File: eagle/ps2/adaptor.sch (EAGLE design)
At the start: 9 parts, among them T1 BSS138, T3 BSS138

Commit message: updated
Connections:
- net CLK_3V3: now also JP1.2; no longer JP1.1
- net DATA_3V3: now also JP1.1; no longer JP1.2
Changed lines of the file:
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@@
 </segment>
 <segment>
-<pinref part="JP1" gate="A" pin="1"/>
-<wire x1="73.66" y1="78.74" x2="73.66" y2="88.9" width="0.1524" layer="91"/>
-<label x="73.152" y="89.154" size="1.778" layer="95" rot="R90"/>
+<pinref part="JP1" gate="A" pin="2"/>
+<wire x1="81.28" y1="78.74" x2="81.28" y2="88.9" width="0.1524" layer="91"/>
+<label x="81.026" y="88.9" size="1.778" layer="95" rot="R90"/>
 </segment>
 </net>
@@
 </segment>
 <segment>
-<pinref part="JP1" gate="A" pin="2"/>
-<wire x1="81.28" y1="78.74" x2="81.28" y2="88.9" width="0.1524" layer="91"/>
-<label x="81.026" y="88.9" size="1.778" layer="95" rot="R90"/>
+<pinref part="JP1" gate="A" pin="1"/>
+<wire x1="73.66" y1="78.74" x2="73.66" y2="88.9" width="0.1524" layer="91"/>
+<label x="73.152" y="89.154" size="1.778" layer="95" rot="R90"/>
 </segment>
 </net>

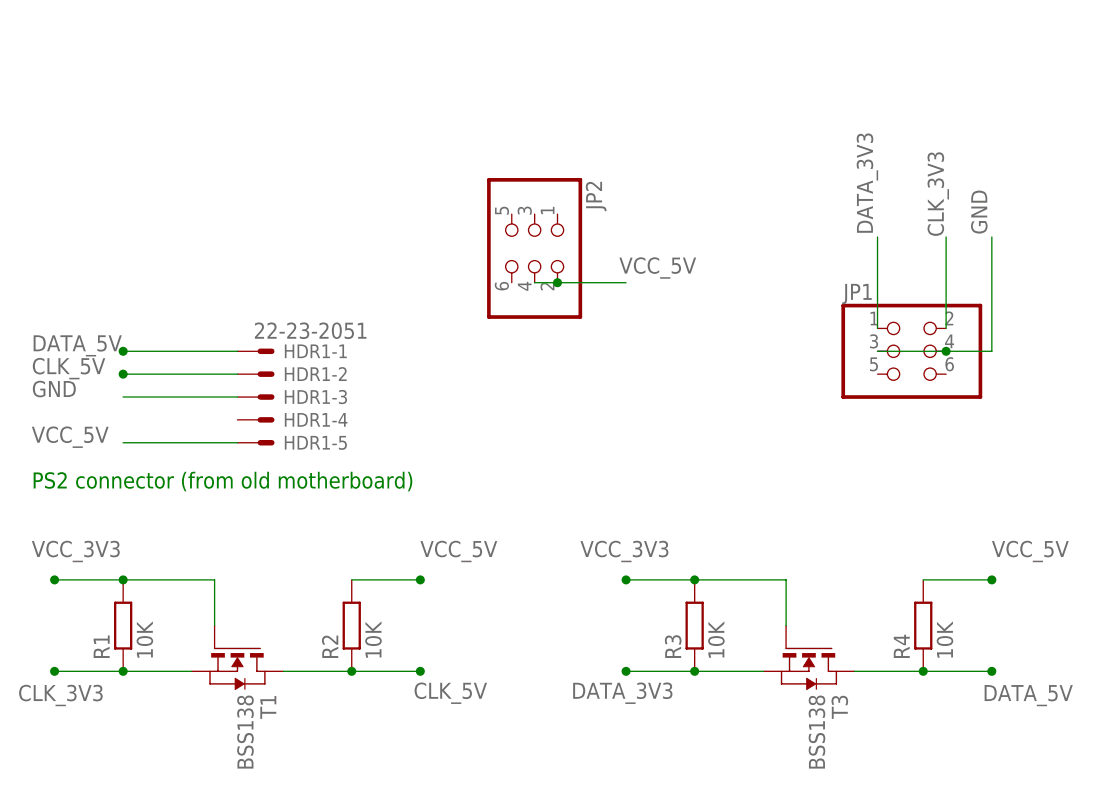
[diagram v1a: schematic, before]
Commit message: nicer connections
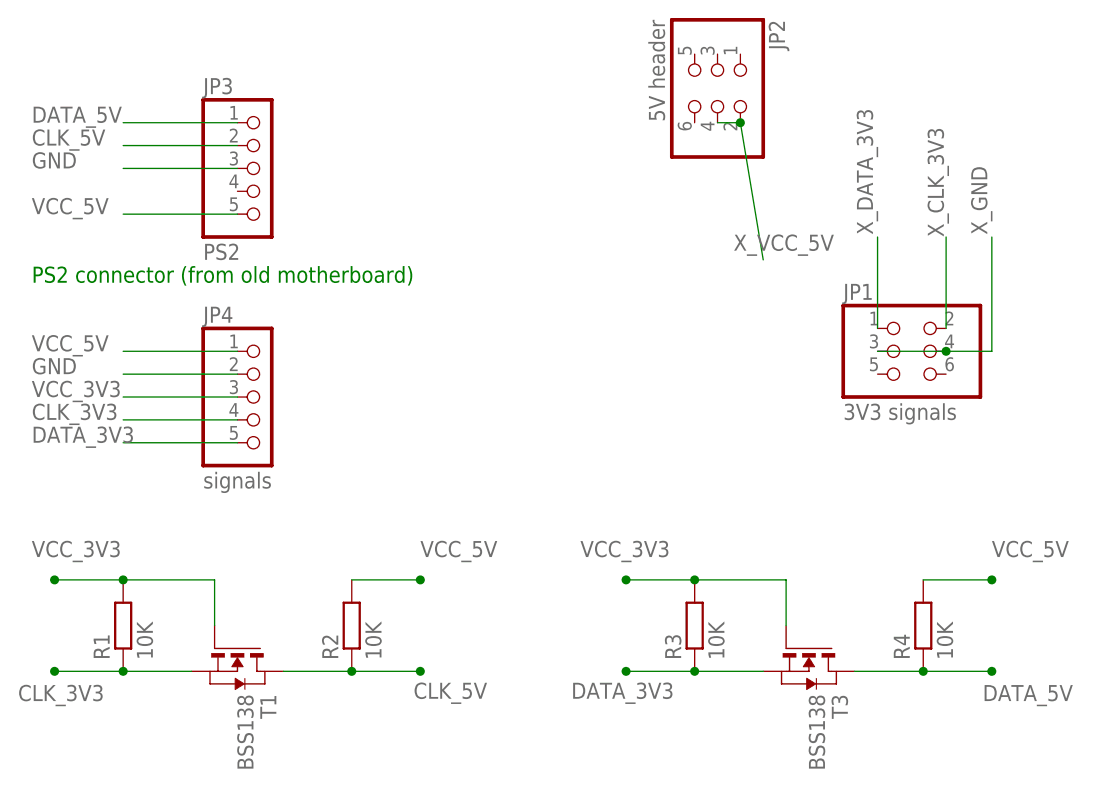
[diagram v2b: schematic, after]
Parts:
- removed HDR1: 22-23-2051, con-molex:22-23-2051
- added JP3: PS2, pinhead:PINHD-1X5
- added JP4: signals, pinhead:PINHD-1X5
- JP1: value (none) -> 3V3 signals
- JP2: value (none) -> 5V header
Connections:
- new net X_CLK_3V3: JP1.2
- new net X_DATA_3V3: JP1.1
- new net X_GND: JP1.3, JP1.4
- new net X_VCC_5V: JP2.2, JP2.4
- net CLK_3V3: now also JP4.4; no longer JP1.2
- net CLK_5V: now also JP3.2; no longer HDR1-2.S
- net DATA_3V3: now also JP4.5; no longer JP1.1
- net DATA_5V: now also JP3.1; no longer HDR1-1.S
- net GND: now also JP3.3, JP4.2; no longer HDR1-3.S, JP1.3, JP1.4
- net VCC_3V3: now also JP4.3
- net VCC_5V: now also JP3.5, JP4.1; no longer HDR1-5.S, JP2.2, JP2.4
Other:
- moved on the sheet: JP2
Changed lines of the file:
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@@
 </variantdefs>
 <classes>
-<class number="0" name="default" width="0" drill="0">
+<class number="0" name="default" width="0.25" drill="0">
+<clearance class="0" value="0.24"/>
+</class>
+<class number="1" name="power" width="0.5" drill="1.1">
+<clearance class="1" value="0.24"/>
 </class>
 </classes>
 <parts>
-<part name="HDR1" library="con-molex" deviceset="22-23-2051" device=""/>
 <part name="T1" library="zetex" deviceset="NMOSSOT23" device="" value="BSS138"/>
 <part name="R1" library="rcl" deviceset="R-EU_" device="R0805" value="10K"/>
@@
 <part name="R3" library="rcl" deviceset="R-EU_" device="R0805" value="10K"/>
 <part name="R4" library="rcl" deviceset="R-EU_" device="R0805" value="10K"/>
-<part name="JP1" library="pinhead" deviceset="PINHD-2X3" device=""/>
-<part name="JP2" library="pinhead" deviceset="PINHD-2X3" device=""/>
+<part name="JP1" library="pinhead" deviceset="PINHD-2X3" device="" value="3V3 signals"/>
+<part name="JP2" library="pinhead" deviceset="PINHD-2X3" device="" value="5V header"/>
+<part name="JP3" library="pinhead" deviceset="PINHD-1X5" device="" value="PS2"/>
+<part name="JP4" library="pinhead" deviceset="PINHD-1X5" device="" value="signals"/>
 </parts>
 <sheets>
 <sheet>
 <plain>
-<text x="-20.32" y="60.96" size="1.778" layer="91">PS2 connector (from old motherboard)</text>
+<text x="-20.32" y="83.82" size="1.778" layer="91">PS2 connector (from old motherboard)</text>
 </plain>
 <instances>
-<instance part="HDR1" gate="-1" x="5.08" y="76.2"/>
-<instance part="HDR1" gate="-2" x="5.08" y="73.66"/>
-<instance part="HDR1" gate="-3" x="5.08" y="71.12"/>
-<instance part="HDR1" gate="-4" x="5.08" y="68.58"/>
-<instance part="HDR1" gate="-5" x="5.08" y="66.04"/>
 <instance part="T1" gate="A" x="2.54" y="40.64" rot="R270"/>
 <instance part="R1" gate="G$1" x="-10.16" y="45.72" rot="R90"/>
@@
 <instance part="R4" gate="G$1" x="78.74" y="45.72" rot="R90"/>
 <instance part="JP1" gate="A" x="76.2" y="76.2"/>
-<instance part="JP2" gate="A" x="35.56" y="88.9" rot="R270"/>
+<instance part="JP2" gate="A" x="55.88" y="106.68" rot="R270"/>
+<instance part="JP3" gate="A" x="5.08" y="96.52"/>
+<instance part="JP4" gate="A" x="5.08" y="71.12"/>
 </instances>
 <busses>
@@
 <nets>
 <net name="DATA_5V" class="0">
-<segment>
-<pinref part="HDR1" gate="-1" pin="S"/>
-<wire x1="2.54" y1="76.2" x2="-10.16" y2="76.2" width="0.1524" layer="91"/>
-<junction x="-10.16" y="76.2"/>
-<label x="-20.32" y="76.2" size="1.778" layer="95"/>
-</segment>
 <segment>
 <pinref part="T3" gate="A" pin="D"/>
@@
 <label x="85.344" y="37.338" size="1.778" layer="95"/>
 </segment>
+<segment>
+<pinref part="JP3" gate="A" pin="1"/>
+<wire x1="2.54" y1="101.6" x2="-10.16" y2="101.6" width="0.1524" layer="91"/>
+<label x="-20.32" y="101.6" size="1.778" layer="95"/>
+</segment>
 </net>
 <net name="CLK_5V" class="0">
-<segment>
-<pinref part="HDR1" gate="-2" pin="S"/>
-<wire x1="2.54" y1="73.66" x2="-10.16" y2="73.66" width="0.1524" layer="91"/>
-<junction x="-10.16" y="73.66"/>
-<label x="-20.32" y="73.66" size="1.778" layer="95"/>
-</segment>
 <segment>
 <pinref part="T1" gate="A" pin="D"/>
@@
 <label x="22.098" y="37.592" size="1.778" layer="95"/>
 </segment>
-</net>
-<net name="GND" class="0">
-<segment>
-<pinref part="JP1" gate="A" pin="3"/>
-<pinref part="JP1" gate="A" pin="4"/>
-<wire x1="73.66" y1="76.2" x2="81.28" y2="76.2" width="0.1524" layer="91"/>
-<wire x1="81.28" y1="76.2" x2="86.36" y2="76.2" width="0.1524" layer="91"/>
-<junction x="81.28" y="76.2"/>
-<wire x1="86.36" y1="76.2" x2="86.36" y2="88.9" width="0.1524" layer="91"/>
-<label x="85.852" y="89.154" size="1.778" layer="95" rot="R90"/>
-</segment>
-<segment>
-<pinref part="HDR1" gate="-3" pin="S"/>
-<wire x1="2.54" y1="71.12" x2="-10.16" y2="71.12" width="0.1524" layer="91"/>
-<label x="-20.32" y="71.12" size="1.778" layer="95"/>
-</segment>
-</net>
-<net name="VCC_5V" class="0">
+<segment>
+<pinref part="JP3" gate="A" pin="2"/>
+<wire x1="-10.16" y1="99.06" x2="2.54" y2="99.06" width="0.1524" layer="91"/>
+<label x="-20.32" y="99.06" size="1.778" layer="95"/>
+</segment>
+</net>
+<net name="GND" class="1">
+<segment>
+<pinref part="JP3" gate="A" pin="3"/>
+<wire x1="-10.16" y1="96.52" x2="2.54" y2="96.52" width="0.1524" layer="91"/>
+<label x="-20.32" y="96.52" size="1.778" layer="95"/>
+</segment>
+<segment>
+<pinref part="JP4" gate="A" pin="2"/>
+<wire x1="-10.16" y1="73.66" x2="2.54" y2="73.66" width="0.1524" layer="91"/>
+<label x="-20.32" y="73.66" size="1.778" layer="95"/>
+</segment>
+</net>
+<net name="VCC_5V" class="1">
 <segment>
 <pinref part="R2" gate="G$1" pin="2"/>
@@
 </segment>
 <segment>
-<pinref part="JP2" gate="A" pin="4"/>
-<pinref part="JP2" gate="A" pin="2"/>
-<wire x1="35.56" y1="83.82" x2="38.1" y2="83.82" width="0.1524" layer="91"/>
-<wire x1="38.1" y1="83.82" x2="45.72" y2="83.82" width="0.1524" layer="91"/>
-<junction x="38.1" y="83.82"/>
-<label x="44.958" y="84.836" size="1.778" layer="95"/>
-</segment>
-<segment>
-<pinref part="HDR1" gate="-5" pin="S"/>
-<wire x1="2.54" y1="66.04" x2="-10.16" y2="66.04" width="0.1524" layer="91"/>
-<label x="-20.32" y="66.04" size="1.778" layer="95"/>
-</segment>
-<segment>
 <pinref part="R4" gate="G$1" pin="2"/>
 <wire x1="78.74" y1="50.8" x2="86.36" y2="50.8" width="0.1524" layer="91"/>
@@
 <label x="86.36" y="53.34" size="1.778" layer="95"/>
 </segment>
-</net>
-<net name="VCC_3V3" class="0">
+<segment>
+<pinref part="JP3" gate="A" pin="5"/>
+<wire x1="-10.16" y1="91.44" x2="2.54" y2="91.44" width="0.1524" layer="91"/>
+<label x="-20.32" y="91.44" size="1.778" layer="95"/>
+</segment>
+<segment>
+<pinref part="JP4" gate="A" pin="1"/>
+<wire x1="2.54" y1="76.2" x2="-10.16" y2="76.2" width="0.1524" layer="91"/>
+<label x="-20.32" y="76.2" size="1.778" layer="95"/>
+</segment>
+</net>
+<net name="VCC_3V3" class="1">
 <segment>
 <pinref part="T1" gate="A" pin="G"/>
@@
 <label x="40.64" y="53.34" size="1.778" layer="95"/>
 </segment>
+<segment>
+<pinref part="JP4" gate="A" pin="3"/>
+<wire x1="-10.16" y1="71.12" x2="2.54" y2="71.12" width="0.1524" layer="91"/>
+<label x="-20.32" y="71.12" size="1.778" layer="95"/>
+</segment>
 </net>
 <net name="CLK_3V3" class="0">
@@
 </segment>
 <segment>
-<pinref part="JP1" gate="A" pin="2"/>
-<wire x1="81.28" y1="78.74" x2="81.28" y2="88.9" width="0.1524" layer="91"/>
-<label x="81.026" y="88.9" size="1.778" layer="95" rot="R90"/>
+<pinref part="JP4" gate="A" pin="4"/>
+<wire x1="-10.16" y1="68.58" x2="2.54" y2="68.58" width="0.1524" layer="91"/>
+<label x="-20.32" y="68.58" size="1.778" layer="95"/>
 </segment>
 </net>
@@
 </segment>
 <segment>
+<pinref part="JP4" gate="A" pin="5"/>
+<wire x1="-10.16" y1="66.04" x2="2.54" y2="66.04" width="0.1524" layer="91"/>
+<label x="-20.32" y="66.04" size="1.778" layer="95"/>
+</segment>
+</net>
+<net name="X_VCC_5V" class="1">
+<segment>
+<pinref part="JP2" gate="A" pin="4"/>
+<pinref part="JP2" gate="A" pin="2"/>
+<wire x1="55.88" y1="101.6" x2="58.42" y2="101.6" width="0.1524" layer="91"/>
+<wire x1="58.42" y1="101.6" x2="60.96" y2="86.36" width="0.1524" layer="91"/>
+<junction x="58.42" y="101.6"/>
+<label x="57.658" y="87.376" size="1.778" layer="95"/>
+</segment>
+</net>
+<net name="X_DATA_3V3" class="0">
+<segment>
 <pinref part="JP1" gate="A" pin="1"/>
 <wire x1="73.66" y1="78.74" x2="73.66" y2="88.9" width="0.1524" layer="91"/>
@@
 </segment>
 </net>
+<net name="X_CLK_3V3" class="0">
+<segment>
+<pinref part="JP1" gate="A" pin="2"/>
+<wire x1="81.28" y1="78.74" x2="81.28" y2="88.9" width="0.1524" layer="91"/>
+<label x="81.026" y="88.9" size="1.778" layer="95" rot="R90"/>
+</segment>
+</net>
+<net name="X_GND" class="1">
+<segment>
+<pinref part="JP1" gate="A" pin="3"/>
+<pinref part="JP1" gate="A" pin="4"/>
+<wire x1="73.66" y1="76.2" x2="81.28" y2="76.2" width="0.1524" layer="91"/>
+<wire x1="81.28" y1="76.2" x2="86.36" y2="76.2" width="0.1524" layer="91"/>
+<junction x="81.28" y="76.2"/>
+<wire x1="86.36" y1="76.2" x2="86.36" y2="88.9" width="0.1524" layer="91"/>
+<label x="85.852" y="89.154" size="1.778" layer="95" rot="R90"/>
+</segment>
+</net>

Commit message: changed pin order - nicer now :)
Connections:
- net GND: now also JP4.3; no longer JP4.2
- net VCC_3V3: now also JP4.2; no longer JP4.3
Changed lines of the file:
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@@
 </segment>
 <segment>
-<pinref part="JP4" gate="A" pin="2"/>
-<wire x1="-10.16" y1="73.66" x2="2.54" y2="73.66" width="0.1524" layer="91"/>
-<label x="-20.32" y="73.66" size="1.778" layer="95"/>
+<pinref part="JP4" gate="A" pin="3"/>
+<wire x1="-10.16" y1="71.12" x2="2.54" y2="71.12" width="0.1524" layer="91"/>
+<label x="-20.32" y="71.12" size="1.778" layer="95"/>
 </segment>
 </net>
@@
 </segment>
 <segment>
-<pinref part="JP4" gate="A" pin="3"/>
-<wire x1="-10.16" y1="71.12" x2="2.54" y2="71.12" width="0.1524" layer="91"/>
-<label x="-20.32" y="71.12" size="1.778" layer="95"/>
+<pinref part="JP4" gate="A" pin="2"/>
+<wire x1="-10.16" y1="73.66" x2="2.54" y2="73.66" width="0.1524" layer="91"/>
+<label x="-20.32" y="73.66" size="1.778" layer="95"/>
 </segment>
 </net>

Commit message: layout fiddling
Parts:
- removed JP1: 3V3 signals, pinhead:PINHD-2X3
- removed JP2: 5V header, pinhead:PINHD-2X3
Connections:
- removed net X_CLK_3V3: JP1.2
- removed net X_DATA_3V3: JP1.1
- removed net X_GND: JP1.3, JP1.4
- removed net X_VCC_5V: JP2.2, JP2.4
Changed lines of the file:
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@@
 <part name="R3" library="rcl" deviceset="R-EU_" device="R0805" value="10K"/>
 <part name="R4" library="rcl" deviceset="R-EU_" device="R0805" value="10K"/>
-<part name="JP1" library="pinhead" deviceset="PINHD-2X3" device="" value="3V3 signals"/>
-<part name="JP2" library="pinhead" deviceset="PINHD-2X3" device="" value="5V header"/>
 <part name="JP3" library="pinhead" deviceset="PINHD-1X5" device="" value="PS2"/>
 <part name="JP4" library="pinhead" deviceset="PINHD-1X5" device="" value="signals"/>
@@
 <instance part="R3" gate="G$1" x="53.34" y="45.72" rot="R90"/>
 <instance part="R4" gate="G$1" x="78.74" y="45.72" rot="R90"/>
-<instance part="JP1" gate="A" x="76.2" y="76.2"/>
-<instance part="JP2" gate="A" x="55.88" y="106.68" rot="R270"/>
 <instance part="JP3" gate="A" x="5.08" y="96.52"/>
 <instance part="JP4" gate="A" x="5.08" y="71.12"/>
@@
 </segment>
 </net>
-<net name="X_VCC_5V" class="1">
-<segment>
-<pinref part="JP2" gate="A" pin="4"/>
-<pinref part="JP2" gate="A" pin="2"/>
-<wire x1="55.88" y1="101.6" x2="58.42" y2="101.6" width="0.1524" layer="91"/>
-<wire x1="58.42" y1="101.6" x2="60.96" y2="86.36" width="0.1524" layer="91"/>
-<junction x="58.42" y="101.6"/>
-<label x="57.658" y="87.376" size="1.778" layer="95"/>
-</segment>
-</net>
-<net name="X_DATA_3V3" class="0">
-<segment>
-<pinref part="JP1" gate="A" pin="1"/>
-<wire x1="73.66" y1="78.74" x2="73.66" y2="88.9" width="0.1524" layer="91"/>
-<label x="73.152" y="89.154" size="1.778" layer="95" rot="R90"/>
-</segment>
-</net>
-<net name="X_CLK_3V3" class="0">
-<segment>
-<pinref part="JP1" gate="A" pin="2"/>
-<wire x1="81.28" y1="78.74" x2="81.28" y2="88.9" width="0.1524" layer="91"/>
-<label x="81.026" y="88.9" size="1.778" layer="95" rot="R90"/>
-</segment>
-</net>
-<net name="X_GND" class="1">
-<segment>
-<pinref part="JP1" gate="A" pin="3"/>
-<pinref part="JP1" gate="A" pin="4"/>
-<wire x1="73.66" y1="76.2" x2="81.28" y2="76.2" width="0.1524" layer="91"/>
-<wire x1="81.28" y1="76.2" x2="86.36" y2="76.2" width="0.1524" layer="91"/>
-<junction x="81.28" y="76.2"/>
-<wire x1="86.36" y1="76.2" x2="86.36" y2="88.9" width="0.1524" layer="91"/>
-<label x="85.852" y="89.154" size="1.778" layer="95" rot="R90"/>
-</segment>
-</net>
